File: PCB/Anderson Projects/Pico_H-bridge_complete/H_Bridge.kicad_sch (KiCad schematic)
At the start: 35 parts, among them J4 2.54 header, Q1 AO3400A, Q2 AO3400A, Q3 DMP3130LQ-7, Q4 DMP3130LQ-7, Q5 MMBT3904, Q6 MMBT3904, Q7 MMBT3904, Q8 MMBT3904, U10 SN74LVC1G14DBV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

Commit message: Gerber files for Pico_H-bridge_complete v1 generated
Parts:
- D3, D4: LCSC C2297 -> C2295
- Q7: footprint Package_TO_SOT_SMD:TO-252-2 -> Package_TO_SOT_SMD:SOT-23
- R22, R29: value 200Ω -> 150Ω; footprint Resistor_SMD:R_0603_1608Metric -> Resistor_SMD:R_0805_2012Metric_Pad1.20x1.40mm_HandSolder; LCSC C17540 -> C17471
- R23, R30: footprint Resistor_SMD:R_0603_1608Metric -> Resistor_SMD:R_0805_2012Metric_Pad1.20x1.40mm_HandSolder
- R28, R35: footprint Resistor_SMD:R_0603_1608Metric -> Resistor_SMD:R_0805_2012Metric_Pad1.20x1.40mm_HandSolder; LCSC C25804 -> C17414
- R7, R9: footprint Resistor_SMD:R_0603_1608Metric -> Resistor_SMD:R_0805_2012Metric_Pad1.20x1.40mm_HandSolder; LCSC C13167 -> C17530

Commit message: Anderson Motor Interface Board v2 complete and ordered.
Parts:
- D3, D4: value LED_G -> LED_Y; LCSC C2295 -> C2296
- Q3, Q4: value DMP3130LQ-7 -> DMP3099L-7; LCSC C461084 -> C155244
- R22, R29: value 150Ω -> 150
- R23, R30: value 1kΩ -> 1k
- R26, R27, R31, R8: value 22kΩ -> 22k
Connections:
- net +5V: no longer JP1.3 (B)
- net Fwd/Rev: now also R26.1; no longer R27.1
- net CCW1 renamed CW1
- net CW1: now also R27.1; no longer R26.1
- new net External PWM: JP1.3 (B)
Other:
- note added: "CW1 and CCW1 have inverted logic (0v is ON, 5v is OFF) FWD/REV PWM CW0 CW1 CCW0 CCW1 0 0 OFF OFF(1) OFF ON(0) 0 1 OFF OFF(1) ON ON(0) 1 1 ON ON(0) OFF OFF(1)"
- moved on the sheet: C4, C5, C8, D3, D4, J4, JP1, Q1, Q2, Q3, Q4, Q5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

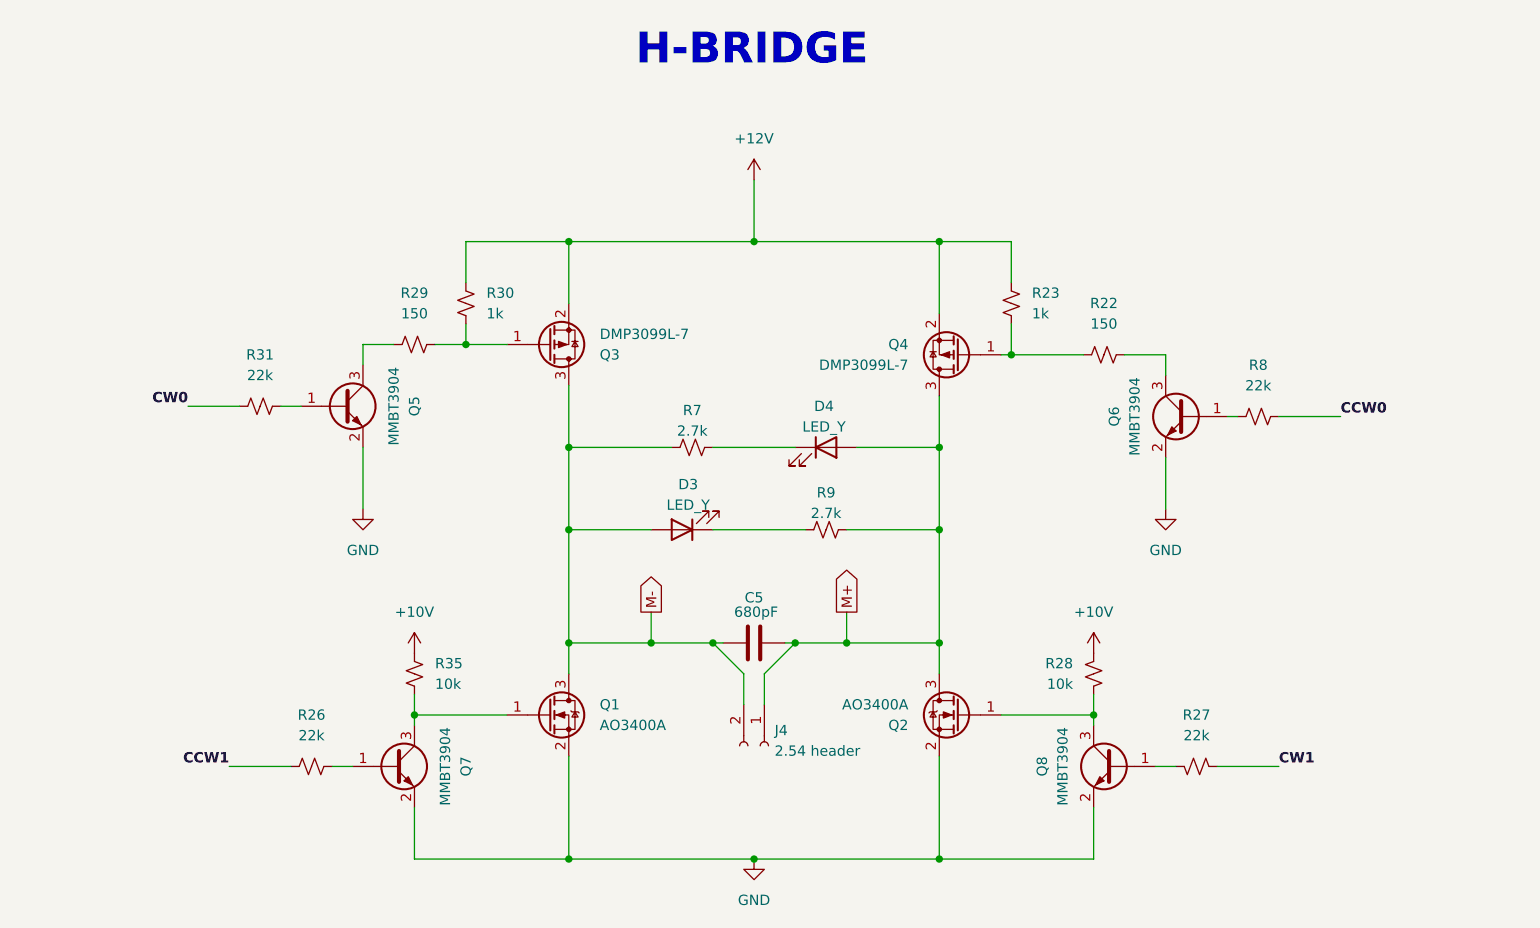
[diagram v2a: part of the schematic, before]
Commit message: Anderson Motor Interface Board v3. - Bengal eyes LED for both directions - heatsink pads on back of board - DIN rail mount Added Heater Box Schematic files in Documentation
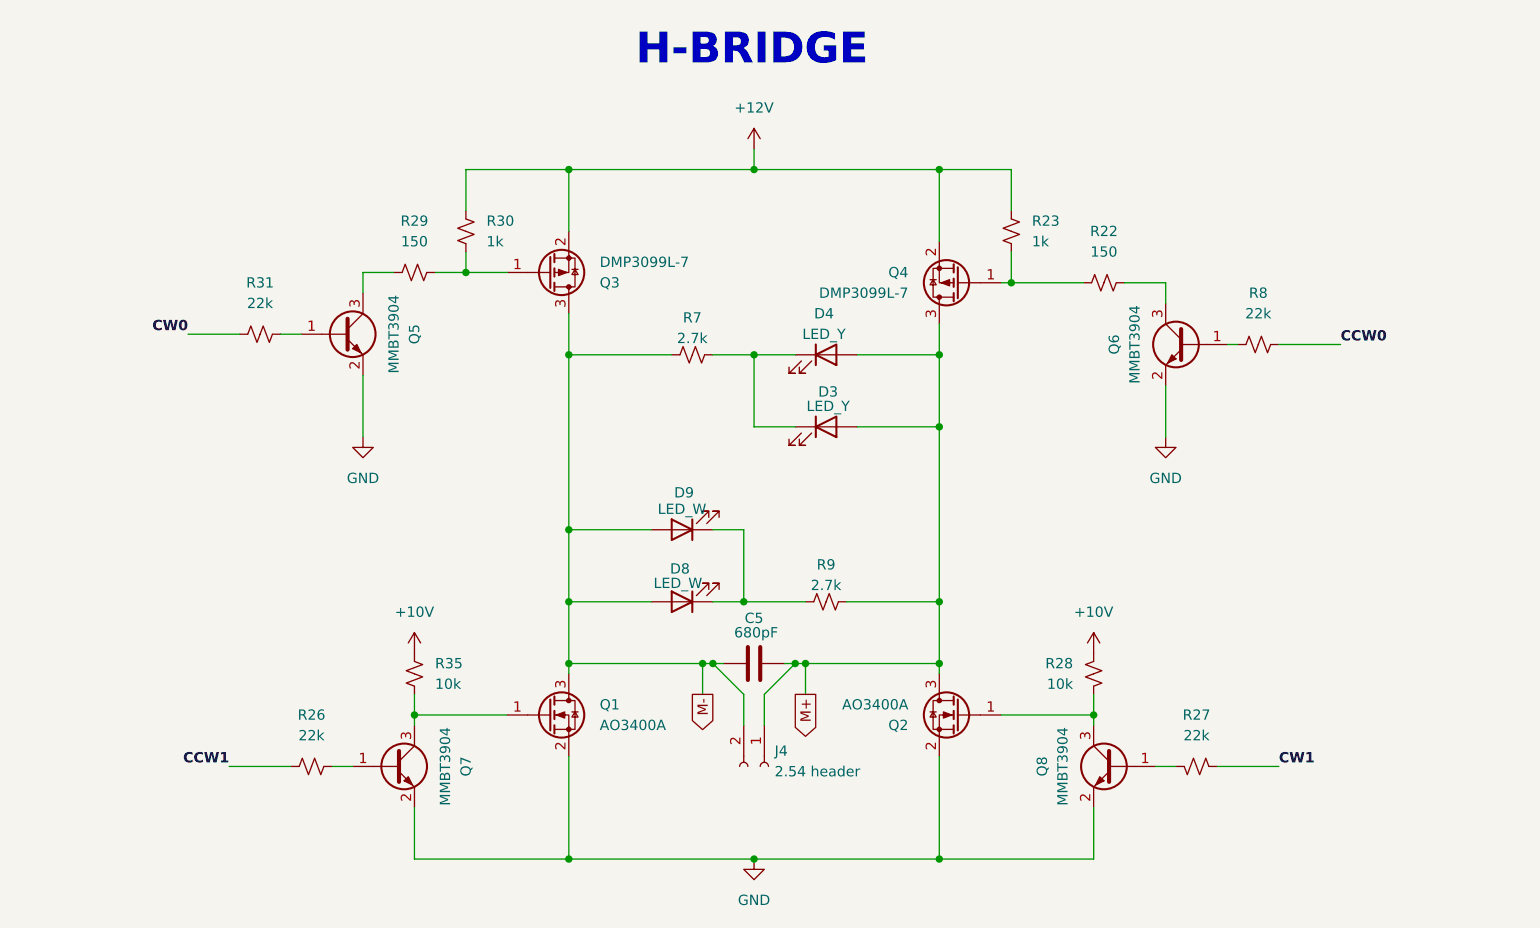
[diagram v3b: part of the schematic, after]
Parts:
- added D8, D9: LED_W, LED_SMD:LED_0603_1608Metric, symbol Device:LED
- D3, D4: footprint LED_SMD:LED_0805_2012Metric -> LED_SMD:LED_0603_1608Metric; LCSC C2296 -> C2286
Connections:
- net M+: now also D3.2 (A)
- net M-: now also D8.2 (A), D9.2 (A); no longer D3.2 (A)
- net at R9.2: now also D8.1 (K), D9.1 (K); no longer D3.1 (K)
- net at D4.1 (K), R7.1: now also D3.1 (K)
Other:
- moved on the sheet: C5, D3, D4, J4, Q3, Q4, Q5, Q6, R22, R23, R29, R30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
